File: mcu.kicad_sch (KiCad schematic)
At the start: 83 parts, among them P20 HEADER-2x11, P22 HEADER-2x13, P26 LPC_JTAG, P28 HEADER-2x11, SW1 SWITCH, SW2 SWITCH, U20 W25Q32, U23 LPC4330FET180, X2 MCU_XTAL, X3 RTC_XTAL

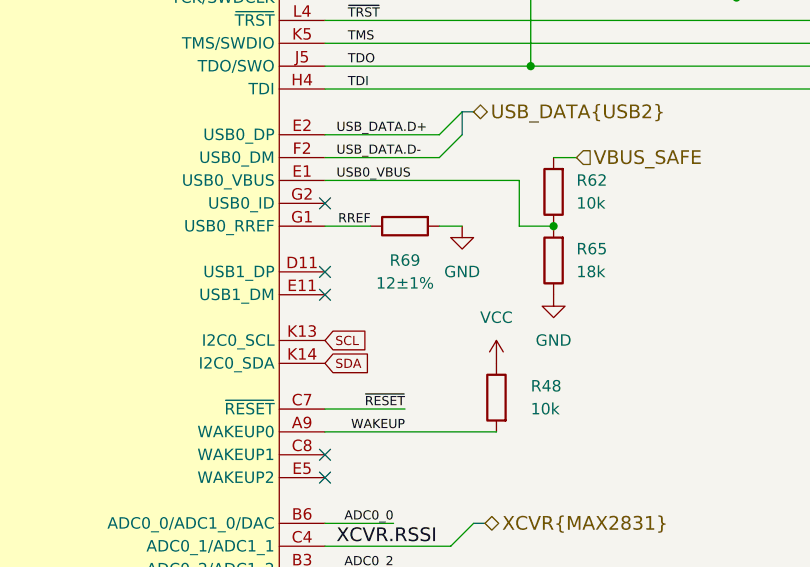
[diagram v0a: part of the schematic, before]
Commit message: Correct component metadata
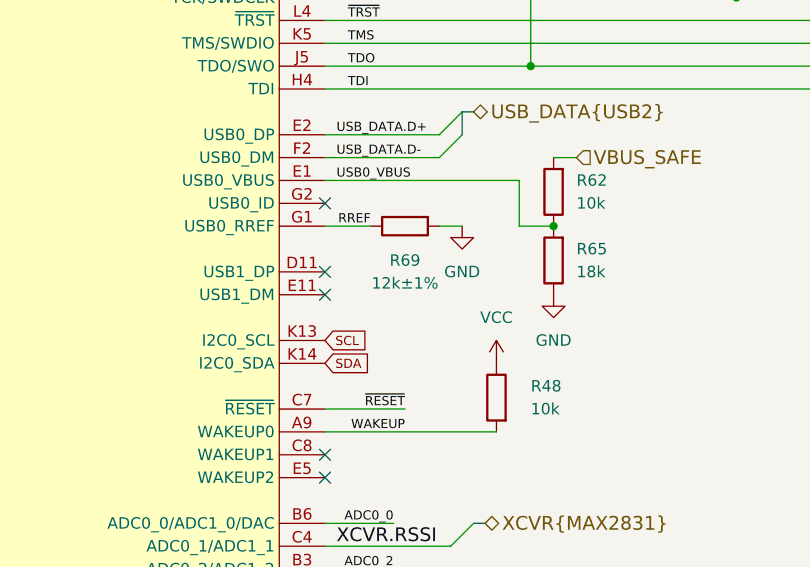
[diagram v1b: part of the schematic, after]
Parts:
- R69: value 12±1% -> 12k±1%
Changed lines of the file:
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@@
 			)
 		)
-		(property "Value" "12±1%"
+		(property "Value" "12k±1%"
 			(at 254 184.15 90)
 			(effects

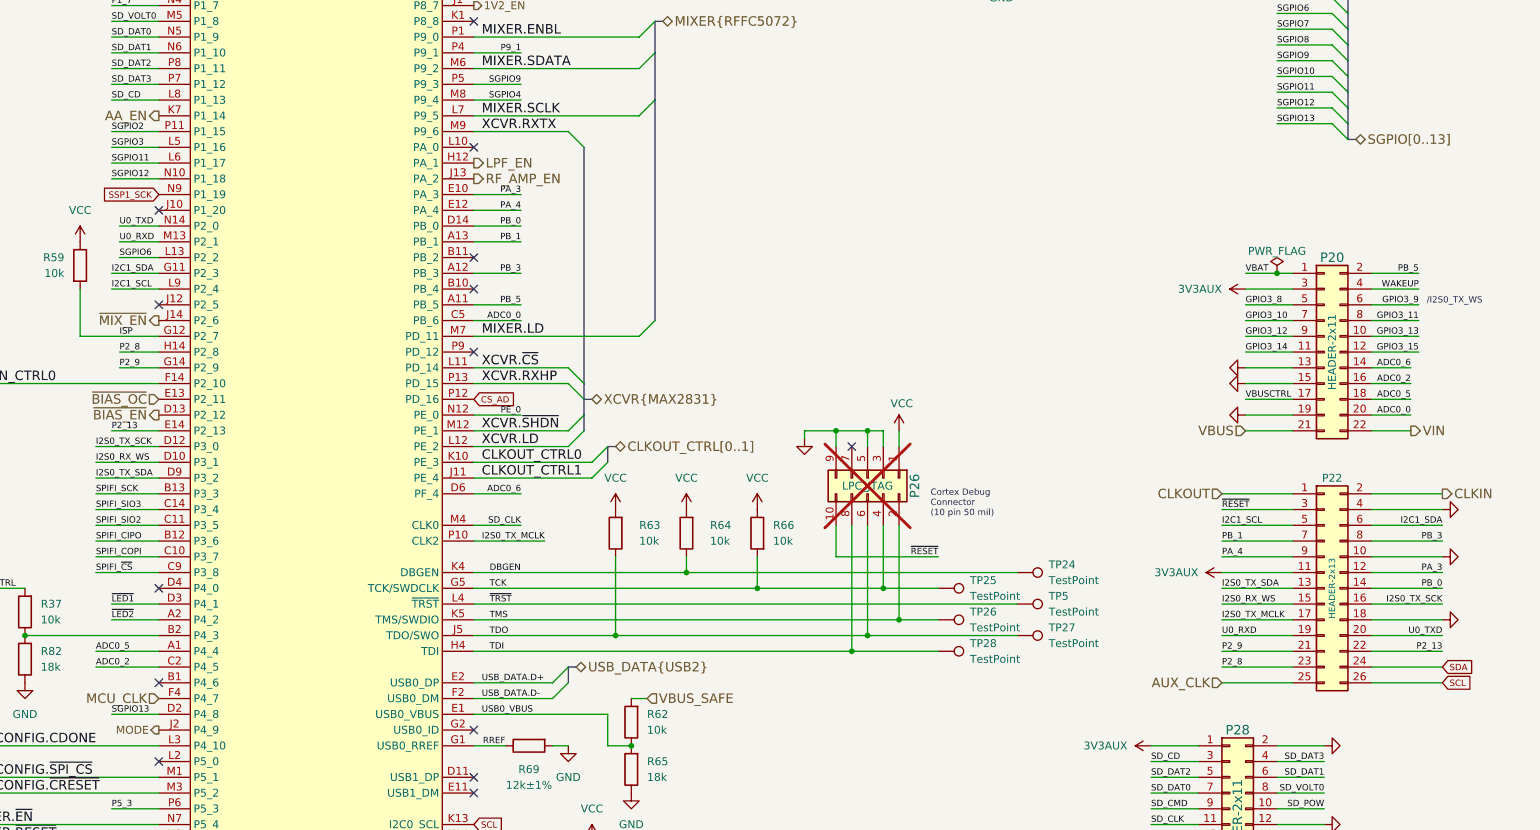
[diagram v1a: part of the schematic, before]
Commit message: Add FPGA_CLK clock generator output
- Remove TRIGGER_EN signal, to be replaced with SPI command
- Reassign clock generator outputs for CLKOUT and CLKIN
- Reassign various FPGA pins
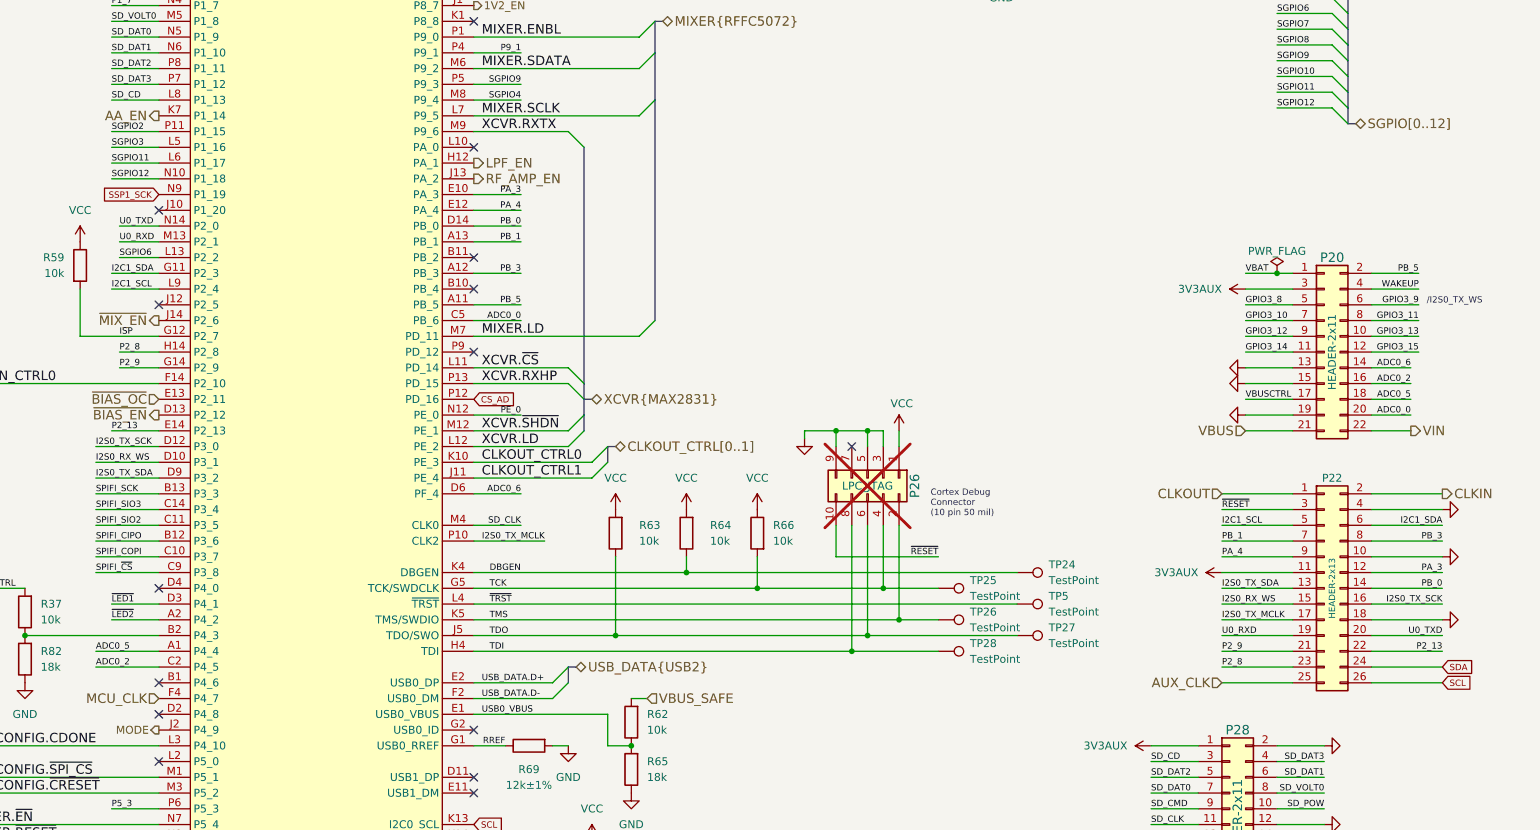
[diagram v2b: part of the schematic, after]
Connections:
- net SGPIO13: no longer names the net of U23.D2 (P4_8)
- no-connect marks 25 -> 26
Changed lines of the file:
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@@
 	)
 	(no_connect
+		(at 194.31 172.72)
+	)
+	(no_connect
 		(at 245.11 114.3)
 	)
@@
 	)
 	(bus_entry
-		(at 383.54 77.47)
-		(size 2.54 2.54)
-		(stroke
-			(width 0)
-			(type default)
-		)
-	)
-	(bus_entry
 		(at 154.94 195.58)
 		(size 2.54 -2.54)
@@
 	(wire
 		(pts
-			(xy 186.69 172.72) (xy 194.31 172.72)
-		)
-		(stroke
-			(width 0)
-			(type default)
-		)
-	)
-	(wire
-		(pts
 			(xy 184.15 149.86) (xy 194.31 149.86)
 		)
@@
 		)
 	)
-	(bus
-		(pts
-			(xy 386.08 77.47) (xy 386.08 80.01)
-		)
-		(stroke
-			(width 0)
-			(type default)
-		)
-	)
 	(wire
 		(pts
@@
 	(bus
 		(pts
-			(xy 386.08 80.01) (xy 387.35 80.01)
+			(xy 386.08 77.47) (xy 387.35 77.47)
 		)
 		(stroke
@@
 	(wire
 		(pts
-			(xy 374.65 77.47) (xy 383.54 77.47)
-		)
-		(stroke
-			(width 0)
-			(type default)
-		)
-	)
-	(wire
-		(pts
 			(xy 311.15 142.24) (xy 311.15 152.4)
 		)
@@
 		)
 	)
-	(label "SGPIO13"
-		(at 186.69 172.72 0)
-		(effects
-			(font
-				(size 1.016 1.016)
-			)
-			(justify left bottom)
-		)
-	)
 	(label "~{LED2}"
 		(at 60.96 181.61 90)
@@
 		)
 	)
-	(label "SGPIO13"
-		(at 374.65 77.47 0)
-		(effects
-			(font
-				(size 1.016 1.016)
-			)
-			(justify left bottom)
-		)
-	)
 	(label "I2S0_TX_SDA"
 		(at 365.76 152.4 0)
@@
 		)
 	)
-	(hierarchical_label "SGPIO[0..13]"
+	(hierarchical_label "SGPIO[0..12]"
 		(shape bidirectional)
-		(at 387.35 80.01 0)
+		(at 387.35 77.47 0)
 		(effects
 			(font

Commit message: Standardize component Value fields
Use Tolerance field instead of expressing tolerance in Value field
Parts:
- C110, C124, C128, C129, C130, C131, C132, C133, C134, C135, C136, C137, C138, C140, C144, C162, C80, C81: value 1uF -> 1 uF
- C118, C157, C158, C164: value 18pF -> 18 pF
- P20, P28: value HEADER-2x11 -> HEADER_2x11
- P22: value HEADER-2x13 -> HEADER_2x13
- R38: value 180k±1% -> 180k; Tolerance (none) -> ±1%
- R39: value 15.4k±1% -> 15.4k; Tolerance (none) -> ±1%
- R69: value 12k±1% -> 12k; Tolerance (none) -> ±1%
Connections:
- net XCVR.LD: now also U23.M9 (P9_6); no longer U23.L12 (PE_2)
- net XCVR.RXTX: now also U23.L12 (PE_2); no longer U23.M9 (P9_6)
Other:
- moved on the sheet: C118, C128, C129, C130, C131, C132, C133, C134, C135, C137, C138, C164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

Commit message: Tune mixer output bias and balun
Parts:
- R19, R30: footprint Resistor_SMD:R_0402_1005Metric -> Resistor_SMD:R_0201_0603Metric; Part Number RC0402JR-0733RL -> RC0201JR-0733RL
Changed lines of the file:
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@@
 			)
 		)
-		(property "Footprint" "Resistor_SMD:R_0402_1005Metric"
+		(property "Footprint" "Resistor_SMD:R_0201_0603Metric"
 			(at 29.21 214.63 0)
 			(effects
@@
 			)
 		)
-		(property "Description" "RES 33 OHM 5% 1/16W 0402"
+		(property "Description" "RES 33 OHM 5% 1/20W 0201"
 			(at 29.21 214.63 0)
 			(effects
@@
 			)
 		)
-		(property "Part Number" "RC0402JR-0733RL"
+		(property "Part Number" "RC0201JR-0733RL"
 			(at 29.21 214.63 0)
 			(effects
@@
 			)
 		)
-		(property "Footprint" "Resistor_SMD:R_0402_1005Metric"
+		(property "Footprint" "Resistor_SMD:R_0201_0603Metric"
 			(at 29.21 240.03 0)
 			(effects
@@
 			)
 		)
-		(property "Description" "RES 33 OHM 5% 1/16W 0402"
+		(property "Description" "RES 33 OHM 5% 1/20W 0201"
 			(at 29.21 240.03 0)
 			(effects
@@
 			)
 		)
-		(property "Part Number" "RC0402JR-0733RL"
+		(property "Part Number" "RC0201JR-0733RL"
 			(at 29.21 240.03 0)
 			(effects

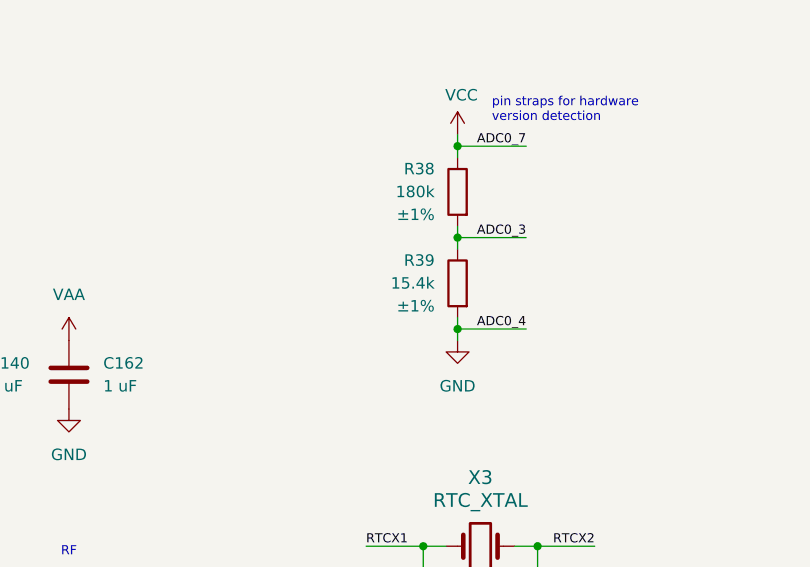
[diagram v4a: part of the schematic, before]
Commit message: Update hardware version detection pin strap
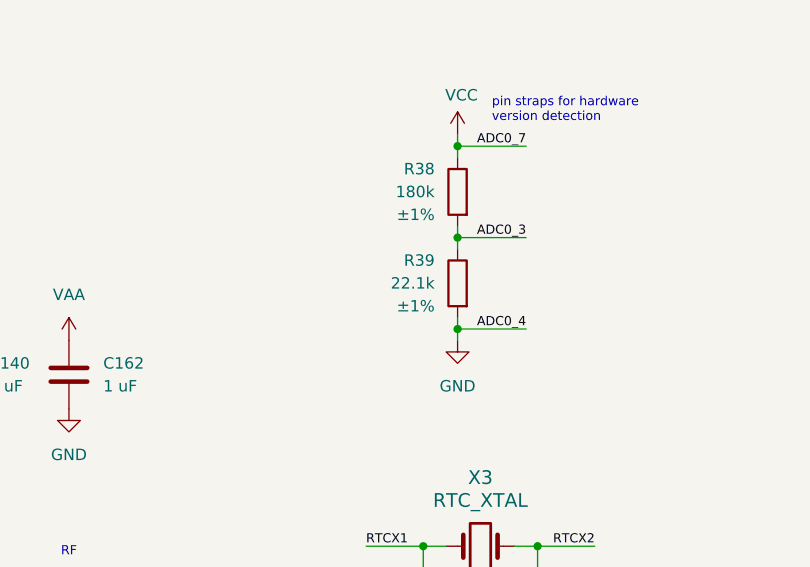
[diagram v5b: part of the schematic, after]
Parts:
- R39: value 15.4k -> 22.1k; Part Number RC0402FR-0715K4L -> RC0402FR-0722K1L
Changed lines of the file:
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@@
 			)
 		)
-		(property "Value" "15.4k"
+		(property "Value" "22.1k"
 			(at 132.08 76.1999 0)
 			(effects
@@
 			)
 		)
-		(property "Description" "RES 15.4K OHM 1% 1/16W 0402"
+		(property "Description" "RES 22.1K OHM 1% 1/16W 0402"
 			(at 134.62 76.2 0)
 			(effects
@@
 			)
 		)
-		(property "Part Number" "RC0402FR-0715K4L"
+		(property "Part Number" "RC0402FR-0722K1L"
 			(at 134.62 76.2 0)
 			(effects

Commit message: Connect trigger and PPS I/O signals to MCU
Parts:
- added R127, R6: 100, Resistor_SMD:R_0201_0603Metric, symbol Device:R
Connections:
- net P6_3 is gone; now on net ~{MIX_EN}: U23.N13 (P6_3)
- net TRIGGER.IN: now also R127.1
- net TRIGGER.OUT: now also R6.2
- net ~{MIX_EN}: no longer U23.J14 (P2_6)
- net P2_5: now reaches U23.J12 (P2_5)
- net at U23.P9 (PD_12): now also R127.2
- new net: R6.1, U23.J14 (P2_6)
- no-connect marks 26 -> 24

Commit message: Move MCU_CLK from CLK7 to CLK2
- Move FPGA_CLK from CLK2 to CLK1, shared with SCT_CLK
- Add AUX_CLK2 on CLK7
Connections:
- net AUX_CLK renamed AUX_CLK2
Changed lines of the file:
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@@
 		)
 	)
-	(hierarchical_label "AUX_CLK"
+	(hierarchical_label "AUX_CLK2"
 		(shape input)
 		(at 365.76 167.64 180)

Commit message: Add CLKIN selector switch
- Rename CLKIN SMA connector to P1
- Rename CLKOUT SMA connector to P2
- Allow selection of CLKIN from either P1 or P22
- Add more signals to P1 mux
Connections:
- net CLKIN_CTRL: now reaches U23.J10 (P1_20)
- net CLKIN renamed P22_CLKIN
- net CLKIN_CTRL0 renamed P1_CTRL0
- net CLKIN_CTRL1 renamed P1_CTRL1
- net CLKIN_CTRL2 renamed P1_CTRL2
- net CLKOUT renamed P2
- net CLKOUT_CTRL0 renamed P2_CTRL0
- net CLKOUT_CTRL1 renamed P2_CTRL1
- no-connect marks 24 -> 23
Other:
- moved on the sheet: R59
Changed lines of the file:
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@@
 	)
 	(no_connect
-		(at 194.31 91.44)
-	)
-	(no_connect
 		(at 245.11 203.2)
 	)
@@
 	(wire
 		(pts
-			(xy 181.61 104.14) (xy 181.61 111.76)
+			(xy 181.61 107.95) (xy 181.61 111.76)
 		)
 		(stroke
@@
 		)
 	)
-	(label "CLKIN_CTRL0"
+	(label "P1_CTRL0"
 		(at 163.83 119.38 0)
 		(effects
@@
 		)
 	)
-	(label "CLKIN_CTRL1"
+	(label "P1_CTRL1"
 		(at 163.83 220.98 0)
 		(effects
@@
 		)
 	)
-	(label "CLKOUT_CTRL1"
+	(label "P2_CTRL1"
 		(at 246.38 134.62 0)
 		(effects
@@
 		)
 	)
-	(label "CLKOUT_CTRL0"
+	(label "P2_CTRL0"
 		(at 246.38 132.08 0)
 		(effects
@@
 		)
 	)
-	(label "CLKIN_CTRL2"
+	(label "P1_CTRL2"
 		(at 163.83 223.52 0)
 		(effects
@@
 		)
 	)
-	(hierarchical_label "CLKOUT"
-		(shape input)
+	(hierarchical_label "P2"
+		(shape bidirectional)
 		(at 365.76 137.16 180)
 		(effects
@@
 		)
 	)
+	(hierarchical_label "CLKIN_CTRL"
+		(shape output)
+		(at 194.31 91.44 180)
+		(effects
+			(font
+				(size 1.524 1.524)
+			)
+			(justify right)
+		)
+	)
 	(hierarchical_label "~{3V3AUX_EN}"
 		(shape output)
@@
 		)
 	)
-	(hierarchical_label "CLKIN_CTRL[0..2]"
-		(shape bidirectional)
+	(hierarchical_label "P1_CTRL[0..2]"
+		(shape output)
 		(at 158.75 226.06 180)
 		(effects
@@
 		)
 	)
-	(hierarchical_label "CLKIN"
+	(hierarchical_label "P22_CLKIN"
 		(shape output)
 		(at 401.32 137.16 0)
@@
 		)
 	)
-	(hierarchical_label "CLKOUT_CTRL[0..1]"
-		(shape bidirectional)
+	(hierarchical_label "P2_CTRL[0..1]"
+		(shape output)
 		(at 267.97 129.54 0)
 		(effects
@@
 	(symbol
 		(lib_id "Device:R")
-		(at 181.61 100.33 0)
+		(at 181.61 104.14 0)
 		(unit 1)
 		(exclude_from_sim no)
@@
 		(fields_autoplaced yes)
 		(property "Reference" "R59"
-			(at 179.07 99.0599 0)
+			(at 179.07 102.8699 0)
 			(effects
 				(font
@@
 		)
 		(property "Value" "10k"
-			(at 179.07 101.5999 0)
+			(at 179.07 105.4099 0)
 			(effects
 				(font
@@
 		)
 		(property "Footprint" "Resistor_SMD:R_0402_1005Metric"
-			(at 181.61 100.33 0)
+			(at 181.61 104.14 0)
 			(effects
 				(font
@@
 		)
 		(property "Datasheet" "~"
-			(at 181.61 100.33 0)
+			(at 181.61 104.14 0)
 			(effects
 				(font
@@
 		)
 		(property "Description" "RES 10K OHM 1/16W 5% 0402 SMD"
-			(at 181.61 100.33 0)
+			(at 181.61 104.14 0)
 			(effects
 				(font
@@
 		)
 		(property "Manufacturer" "Yageo"
-			(at 181.61 100.33 0)
+			(at 181.61 104.14 0)
 			(effects
 				(font
@@
 		)
 		(property "Part Number" "RC0402JR-0710KL"
-			(at 181.61 100.33 0)
+			(at 181.61 104.14 0)
 			(effects
 				(font
@@
 		)
 		(property "Substitution" "any equivalent"
-			(at 181.61 100.33 0)
+			(at 181.61 104.14 0)
 			(effects
 				(font
@@
 	(symbol
 		(lib_id "power:VCC")
-		(at 181.61 96.52 0)
+		(at 181.61 100.33 0)
 		(unit 1)
 		(exclude_from_sim no)
@@
 		(fields_autoplaced yes)
 		(property "Reference" "#PWR0163"
-			(at 181.61 100.33 0)
+			(at 181.61 104.14 0)
 			(effects
 				(font
@@
 		)
 		(property "Value" "VCC"
-			(at 181.61 91.44 0)
+			(at 181.61 95.25 0)
 			(effects
 				(font
@@
 		)
 		(property "Footprint" ""
-			(at 181.61 96.52 0)
+			(at 181.61 100.33 0)
 			(effects
 				(font
@@
 		)
 		(property "Datasheet" ""
-			(at 181.61 96.52 0)
+			(at 181.61 100.33 0)
 			(effects
 				(font
@@
 		)
 		(property "Description" "Power symbol creates a global label with name \"VCC\""
-			(at 181.61 96.52 0)
+			(at 181.61 100.33 0)
 			(effects
 				(font
